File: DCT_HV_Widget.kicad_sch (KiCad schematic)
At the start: 12 parts

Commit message: Updated schematic.
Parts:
- removed D? (x2): BAS21, Package_TO_SOT_SMD:SOT-23, symbol Diode:BAS21
- removed U?: LT1468CS8-PBF, SO-8_S_LIT, symbol LT1468CS8#PBF:LT1468CS8-PBF
- added D1: BAS21SW, symbol Device:D_Dual_Series_ACK_Parallel
- added U?: OC150G, symbol OC150G:OC150G
- added U?: OPAMP, symbol pspice:OPAMP
- gave numbers to parts that had none: 7
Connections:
- net at R4.1: now also C2.1, R2.2, U?.1 (+)
- net at R4.2: now also C2.1
- net VCC: now reaches R3.1
- net VCC: now also R1.1
- net GND: now reaches R3.2
- net GND: now also Q1.3 (C), R2.1, D1.2 (A), U?.3, U?.4 (V+), U?.5 (V-)
- net at C2.2: now also C2.2, Q1.2 (B), U?.3
- net at R?.1: now also Q1.1 (E)
- net at R?.2: now also U?.1
- net at R6.1: now also U?.2 (-)
- net at R6.2: now also R1.2, D1.3 (K)
- new net: U?.2, U?.4
- new net: D1.1 (K), U?.6
- new net HV8k: U?.5
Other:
- moved on the sheet: C2, Q1, R1, R2, R3, R4, R6, R?

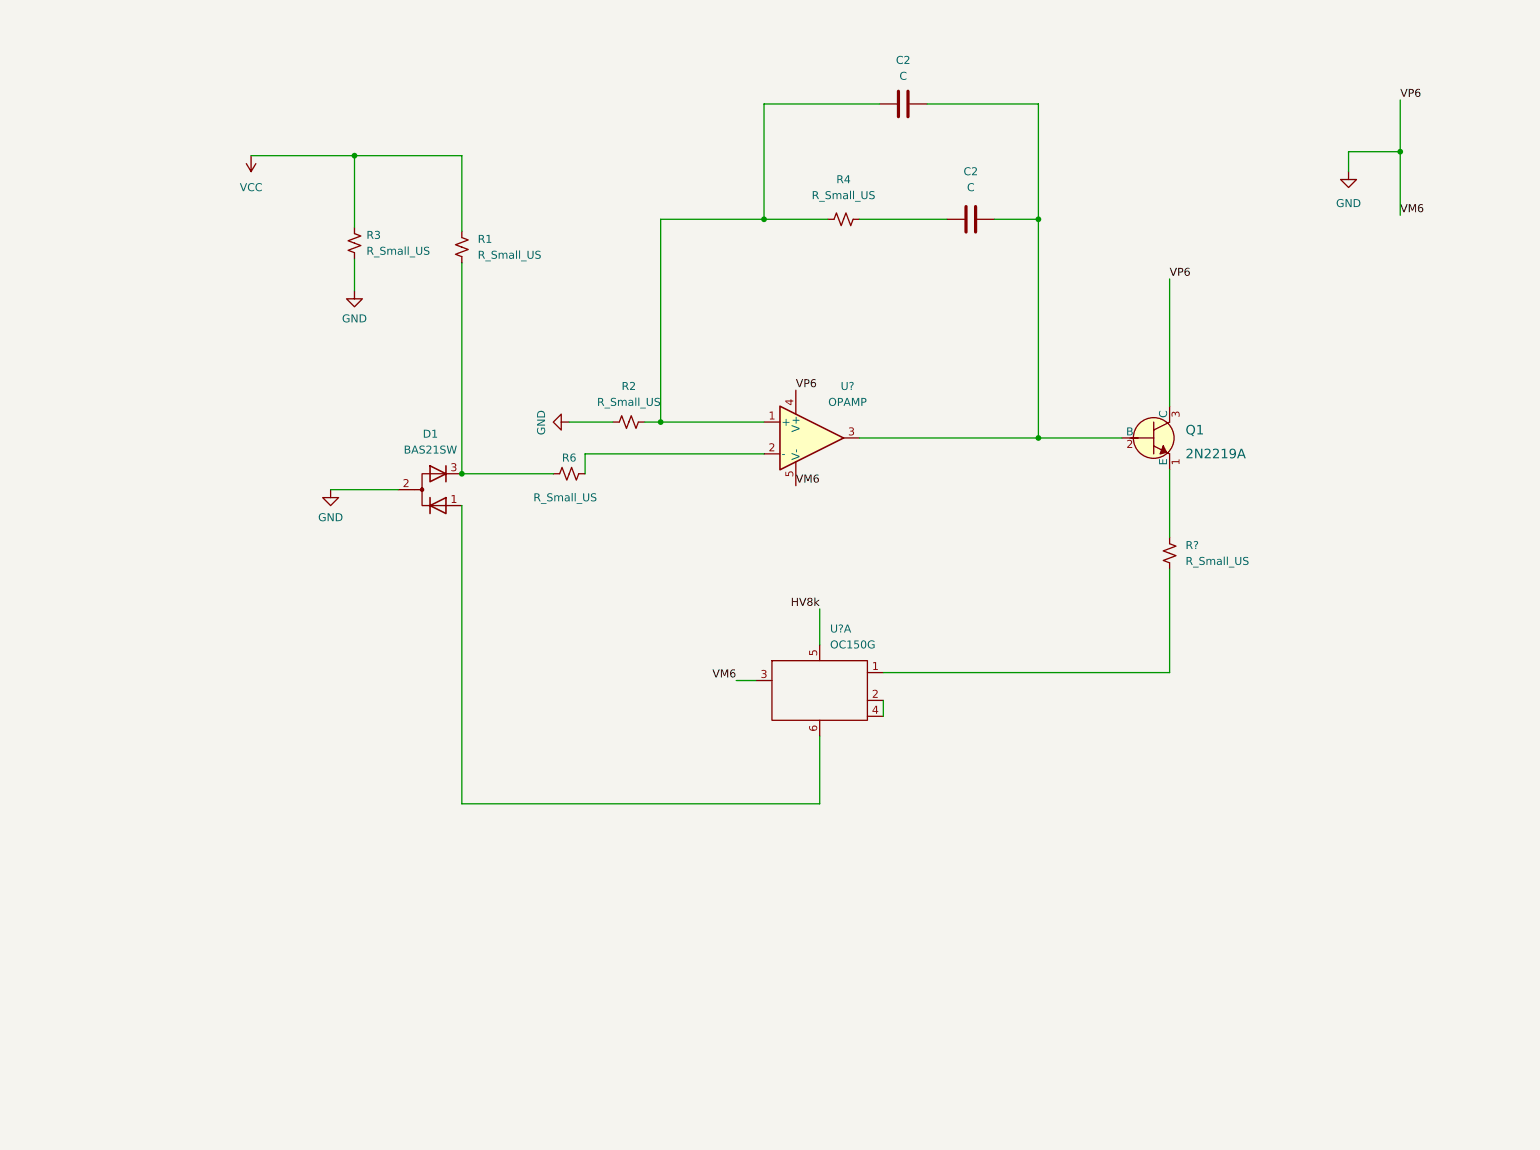
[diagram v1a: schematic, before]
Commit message: Updated schematic connecting pin 3 and pin 1 on BAS21SW diode
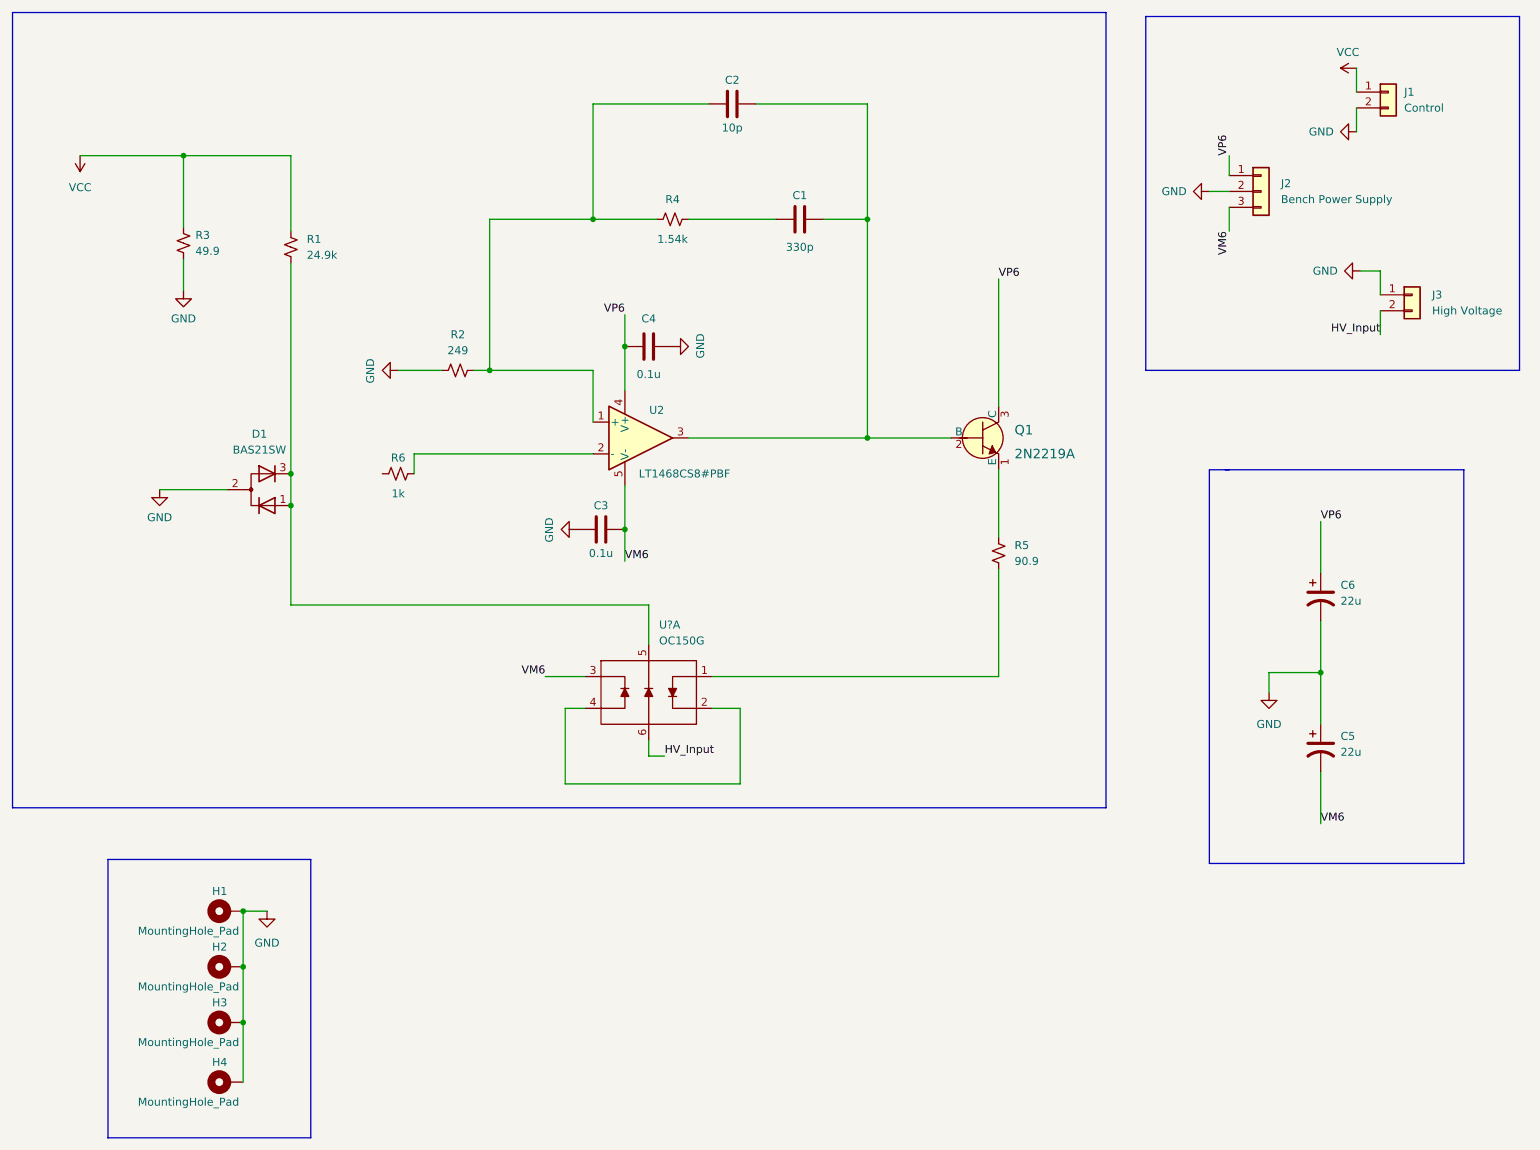
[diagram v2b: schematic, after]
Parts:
- removed U?: OC150G, symbol OC150G:OC150G
- added C3, C4: 0.1u, symbol Device:C
- added C5, C6: 22u, symbol Device:C_Polarized_US
- added H1, H2, H3, H4: MountingHole_Pad, symbol Mechanical:MountingHole_Pad
- added J1: Control, symbol Connector_Generic:Conn_01x02
- added J2: Bench Power Supply, symbol Connector_Generic:Conn_01x03
- added J3: High Voltage, symbol Connector_Generic:Conn_01x02
- added U?: OC150G, symbol OC150G:OC150G
- C1: renamed from C2; value C -> 330p
- C2: value C -> 10p
- R1: value R_Small_US -> 24.9k
- R2: value R_Small_US -> 249
- R3: value R_Small_US -> 49.9
- R4: value R_Small_US -> 1.54k
- R5: renamed from R?; value R_Small_US -> 90.9
- R6: value R_Small_US -> 1k
- U2: renamed from U?; value OPAMP -> LT1468CS8#PBF
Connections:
- net GND: now also C3.1, C4.2, C5.1, C6.2, H1.1, H2.1, H3.1, H4.1, J1.2 (Pin_2), J2.2 (Pin_2), J3.1 (Pin_1); no longer Q1.3 (C), U2.4 (V+), U2.5 (V-)
- net VCC: now also J1.1 (Pin_1)
- net at R5.2: now also U?.1
- net at D1.1 (K): now also D1.3 (K), R1.2, U?.5
- new net: U?.2, U?.4
- new net HV_Input: J3.2 (Pin_2), U?.6
- new net VM6: C3.2, C5.2, J2.3 (Pin_3), U2.5 (V-), U?.3
- new net VP6: C4.1, C6.1, J2.1 (Pin_1), Q1.3 (C), U2.4 (V+)
- now unconnected: R6.2
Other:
- moved on the sheet: C1, C2, Q1, R1, R2, R3, R4, R5, R6, U2

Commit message: Minor change to schematic
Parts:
- Q1: value 2N2219A -> ZXTN10150D
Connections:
- net at D1.1 (K), D1.3 (K), R1.2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: now also R6.2
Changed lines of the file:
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@@
-    (stroke (width 0) (type default) (color 0 0 0 0))
-  )
-  (wire (pts (xy 85.09 89.535) (xy 113.665 89.535))
     (stroke (width 0) (type default) (color 0 0 0 0))
   )
@@
     (stroke (width 0) (type default) (color 0 0 0 0))
   )
-  (wire (pts (xy 85.09 89.535) (xy 85.09 92.71))
-    (stroke (width 0) (type default) (color 0 0 0 0))
-  )
   (wire (pts (xy 132.715 125.095) (xy 178.435 125.095))
     (stroke (width 0) (type default) (color 0 0 0 0))
@@
     (stroke (width 0) (type default) (color 0 0 0 0))
   )
+  (wire (pts (xy 113.665 89.535) (xy 95.885 89.535))
+    (stroke (width 0) (type default) (color 0 0 0 0))
+  )
   (wire (pts (xy 48.26 58.42) (xy 48.26 63.5))
     (stroke (width 0) (type default) (color 0 0 0 0))
@@
     (stroke (width 0) (type default) (color 0 0 0 0))
   )
+  (wire (pts (xy 95.885 92.71) (xy 85.09 92.71))
+    (stroke (width 0) (type default) (color 0 0 0 0))
+  )
+  (wire (pts (xy 65.405 92.71) (xy 80.01 92.71))
+    (stroke (width 0) (type default) (color 0 0 0 0))
+  )
   (wire (pts (xy 229.87 116.205) (xy 229.87 124.46))
     (stroke (width 0) (type default) (color 0 0 0 0))
@@
   )
   (wire (pts (xy 215.265 41.91) (xy 215.265 45.085))
+    (stroke (width 0) (type default) (color 0 0 0 0))
+  )
+  (wire (pts (xy 95.885 89.535) (xy 95.885 92.71))
     (stroke (width 0) (type default) (color 0 0 0 0))
   )
@@
   (symbol (lib_id "dk_Transistors-Bipolar-BJT-Single:2N2219A") (at 175.895 86.995 0) (unit 1)
     (in_bom yes) (on_board yes) (fields_autoplaced)
-    (property "Reference" "Q1" (id 0) (at 180.975 85.725 0)
+    (property "Reference" "Q1" (id 0) (at 180.34 85.725 0)
       (effects (font (size 1.524 1.524)) (justify left))
     )
-    (property "Value" "2N2219A" (id 1) (at 180.975 89.535 0)
+    (property "Value" "ZXTN10150D" (id 1) (at 180.34 89.535 0)
       (effects (font (size 1.524 1.524)) (justify left))
     )
@@
     )
     (path "/8e830ab1-87c7-402f-956c-7d7938416b50"
-      (reference "Q1") (unit 1) (value "2N2219A") (footprint "digikey-footprints:TO-39-3")
+      (reference "Q1") (unit 1) (value "ZXTN10150D") (footprint "digikey-footprints:TO-39-3")
     )
     (path "/d52893e1-9864-4675-8757-03951742d70d"

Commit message: Corrected OpAmp pins and updated LT1468
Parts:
- removed U2: LT1468CS8#PBF, symbol pspice:OPAMP
- added U1: LT1468CS8-PBF, SO-8_S_LIT, symbol LT1468CS8#PBF:LT1468CS8-PBF
- J1: value Control -> Control Voltage
- gave numbers to parts that had none: 1
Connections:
- net VM6: now also U1.4 (V-)
- net VP6: now also U1.7 (V+)
- net at C2.1, R2.2, R4.1: now also U1.2 (-IN)
- net at C1.2, C2.2, Q1.2 (B): now also U1.6 (OUT)
- net at R6.1: now also U1.3 (+IN)
- no-connect marks 0 -> 2
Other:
- note added: "Bench Power Supply"
- note added: "FLoBBr"
- note added: "Mounting Holes"
- note added: "Power Connectors"
- moved on the sheet: C3, C4, Q1

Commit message: Updated OC150G footprint
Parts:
- C1, C2, C3, C4: footprint (none) -> Capacitor_SMD:C_0603_1608Metric
- H1, H2, H3, H4: footprint (none) -> MountingHole:MountingHole_3.2mm_M3_Pad
- Q1: footprint digikey-footprints:TO-39-3 -> (none)
- R1, R2, R3, R4, R5, R6: footprint (none) -> Resistor_SMD:R_0603_1608Metric
- U1: footprint SO-8_S_LIT -> LT1468CS8#PBF:LT1468CS8#PBF_SO-8_S_LIT
- U2: footprint (none) -> DCT_HV_Widget:OC150G

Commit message: Updated PCB layout
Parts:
- C5, C6: footprint (none) -> Capacitor_Tantalum_SMD:CP_EIA-3528-21_Kemet-B
- D1: footprint (none) -> DCT_HV_Widget:BAS21SW
- J1, J3: footprint (none) -> Connector_Molex:Molex_Micro-Fit_3.0_43650-0200_1x02_P3.00mm_Horizontal
- J2: footprint (none) -> Connector_Molex:Molex_Micro-Fit_3.0_43650-0300_1x03_P3.00mm_Horizontal
- Q1: footprint (none) -> DCT_HV_Widget:ZXTN10150DZ
- U2: footprint DCT_HV_Widget:OC150G -> DCT_HV_Widget:OC150G_v2
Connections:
- net GND: now also D1.3 (A); no longer D1.2 (A)
- net at D1.1 (K), R1.2, R6.2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: now also D1.2 (K); no longer D1.3 (K)
- net VCC renamed V_Control
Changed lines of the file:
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@@
     (effects (font (size 1.27 1.27)) (justify left bottom))
+  )
+  (label "V_Control" (at 31.75 41.91 270)
+    (effects (font (size 1.27 1.27)) (justify right bottom))
   )
   (label "VP6" (at 229.87 100.33 0)
@@
     (effects (font (size 1.27 1.27)) (justify left bottom))
   )
+  (label "V_Control" (at 235.585 27.94 180)
+    (effects (font (size 1.27 1.27)) (justify right bottom))
+  )
   (label "VM6" (at 215.265 53.975 270)
     (effects (font (size 1.27 1.27)) (justify right bottom))
@@
   (label "HV_Input" (at 125.095 137.795 0)
     (effects (font (size 1.27 1.27)) (justify left bottom))
+  )
+  (label "V_Input" (at 228.6 40.005 270)
+    (effects (font (size 1.27 1.27)) (justify right bottom))
   )
   (label "VP6" (at 215.265 41.91 90)
@@
     (pin "2")
   )
-  (symbol (lib_id "power:VCC") (at 235.585 27.94 90) (unit 1)
-    (in_bom yes) (on_board yes)
-    (property "Reference" "#PWR0107" (id 0) (at 239.395 27.94 0)
-      (effects (font (size 1.27 1.27)) hide)
-    )
-    (property "Value" "VCC" (id 1) (at 232.41 25.4 90)
-      (effects (font (size 1.27 1.27)) (justify right))
-    )
-    (property "Footprint" "" (id 2) (at 235.585 27.94 0)
-      (effects (font (size 1.27 1.27)) hide)
-    )
-    (property "Datasheet" "" (id 3) (at 235.585 27.94 0)
-      (effects (font (size 1.27 1.27)) hide)
-    )
-    (pin "1")
-  )
   (symbol (lib_id "power:GND") (at 234.95 60.325 0) (unit 1)
     (in_bom yes) (on_board yes)
@@
       (effects (font (size 1.27 1.27)) (justify left))
     )
-    (property "Footprint" "DCT_HV_Widget:OC150G" (id 2) (at 123.571 127.381 0)
+    (property "Footprint" "DCT_HV_Widget:OC150G_v2" (id 2) (at 123.571 127.381 0)
       (effects (font (size 1.27 1.27)) hide)
     )
@@
       (effects (font (size 1.27 1.27)) (justify left))
     )
-    (property "Footprint" "" (id 2) (at 220.345 47.625 0)
+    (property "Footprint" "Connector_Molex:Molex_Micro-Fit_3.0_43650-0300_1x03_P3.00mm_Horizontal" (id 2) (at 220.345 47.625 0)
       (effects (font (size 1.27 1.27)) hide)
     )
@@
       (effects (font (size 1.27 1.27)) (justify left))
     )
-    (property "Footprint" "" (id 2) (at 244.475 64.135 0)
+    (property "Footprint" "Connector_Molex:Molex_Micro-Fit_3.0_43650-0200_1x02_P3.00mm_Horizontal" (id 2) (at 244.475 64.135 0)
       (effects (font (size 1.27 1.27)) hide)
     )
@@
     (property "Reference" "D1" (id 0) (at 60.96 89.535 0))
     (property "Value" "BAS21SW" (id 1) (at 60.325 100.965 0))
-    (property "Footprint" "" (id 2) (at 59.055 95.25 0)
+    (property "Footprint" "DCT_HV_Widget:BAS21SW" (id 2) (at 59.055 95.25 0)
       (effects (font (size 1.27 1.27)) hide)
     )
@@
       (effects (font (size 1.524 1.524)) (justify left))
     )
-    (property "Footprint" "" (id 2) (at 180.975 80.645 0)
+    (property "Footprint" "DCT_HV_Widget:ZXTN10150DZ" (id 2) (at 180.975 80.645 0)
       (effects (font (size 1.524 1.524)) (justify left) hide)
     )
@@
     (pin "2")
     (pin "3")
-  )
-  (symbol (lib_id "power:VCC") (at 31.75 41.91 180) (unit 1)
-    (in_bom yes) (on_board yes) (fields_autoplaced)
-    (property "Reference" "#PWR0110" (id 0) (at 31.75 38.1 0)
-      (effects (font (size 1.27 1.27)) hide)
-    )
-    (property "Value" "VCC" (id 1) (at 31.75 46.99 0))
-    (property "Footprint" "" (id 2) (at 31.75 41.91 0)
-      (effects (font (size 1.27 1.27)) hide)
-    )
-    (property "Datasheet" "" (id 3) (at 31.75 41.91 0)
-      (effects (font (size 1.27 1.27)) hide)
-    )
-    (pin "1")
   )
   (symbol (lib_id "power:GND") (at 48.26 63.5 0) (unit 1)
@@
       (effects (font (size 1.27 1.27)) (justify left))
     )
-    (property "Footprint" "" (id 2) (at 240.665 31.75 0)
+    (property "Footprint" "Connector_Molex:Molex_Micro-Fit_3.0_43650-0200_1x02_P3.00mm_Horizontal" (id 2) (at 240.665 31.75 0)
       (effects (font (size 1.27 1.27)) hide)
     )
@@
       (effects (font (size 1.27 1.27)) (justify left))
     )
-    (property "Footprint" "" (id 2) (at 229.87 112.395 0)
+    (property "Footprint" "Capacitor_Tantalum_SMD:CP_EIA-3528-21_Kemet-B" (id 2) (at 229.87 112.395 0)
       (effects (font (size 1.27 1.27)) hide)
     )
@@
       (effects (font (size 1.27 1.27)) (justify left))
     )
-    (property "Footprint" "" (id 2) (at 229.87 136.525 0)
+    (property "Footprint" "Capacitor_Tantalum_SMD:CP_EIA-3528-21_Kemet-B" (id 2) (at 229.87 136.525 0)
       (effects (font (size 1.27 1.27)) hide)
     )
@@
       (reference "#PWR0106") (unit 1) (value "GND") (footprint "")
     )
-    (path "/57d14982-5bb6-4066-a281-663fb3057bd3"
-      (reference "#PWR0107") (unit 1) (value "VCC") (footprint "")
-    )
     (path "/d7412664-fb55-4327-9567-f6e1a4f37fe6"
       (reference "#PWR0108") (unit 1) (value "GND") (footprint "")
@@
       (reference "#PWR0109") (unit 1) (value "GND") (footprint "")
     )
-    (path "/a7bdbe47-0108-4ab6-a2c9-1cb5ab4bd2e8"
-      (reference "#PWR0110") (unit 1) (value "VCC") (footprint "")
-    )
     (path "/23f6f893-dc24-40ae-95c5-84db8f5f0b0b"
       (reference "#PWR0111") (unit 1) (value "GND") (footprint "")
@@
     )
     (path "/cc10a100-055b-4e9c-97e1-1facb23a1991"
-      (reference "C5") (unit 1) (value "22u") (footprint "")
+      (reference "C5") (unit 1) (value "22u") (footprint "Capacitor_Tantalum_SMD:CP_EIA-3528-21_Kemet-B")
     )
     (path "/c4400881-e5ca-4f2a-be70-c86fa2ddcf32"
-      (reference "C6") (unit 1) (value "22u") (footprint "")
+      (reference "C6") (unit 1) (value "22u") (footprint "Capacitor_Tantalum_SMD:CP_EIA-3528-21_Kemet-B")
     )
     (path "/790c30cd-6531-4300-9b45-833fe1fb861e"
-      (reference "D1") (unit 1) (value "BAS21SW") (footprint "")
+      (reference "D1") (unit 1) (value "BAS21SW") (footprint "DCT_HV_Widget:BAS21SW")
     )
     (path "/1814a377-0806-4e8c-b4a1-f86b9d72b0f6"
@@
     )
     (path "/bdc9f8ac-1856-4424-8824-bbc6c83ee9e4"
-      (reference "J1") (unit 1) (value "Control Voltage") (footprint "")
+      (reference "J1") (unit 1) (value "Control Voltage") (footprint "Connector_Molex:Molex_Micro-Fit_3.0_43650-0200_1x02_P3.00mm_Horizontal")
     )
     (path "/6b30e474-d9ea-4a45-8e0e-1ee5e1f38702"
-      (reference "J2") (unit 1) (value "Bench Power Supply") (footprint "")
+      (reference "J2") (unit 1) (value "Bench Power Supply") (footprint "Connector_Molex:Molex_Micro-Fit_3.0_43650-0300_1x03_P3.00mm_Horizontal")
     )
     (path "/6e5b450c-1a45-4e56-b6dc-f06c19c1d668"
-      (reference "J3") (unit 1) (value "High Voltage") (footprint "")
+      (reference "J3") (unit 1) (value "High Voltage") (footprint "Connector_Molex:Molex_Micro-Fit_3.0_43650-0200_1x02_P3.00mm_Horizontal")
     )
     (path "/8e830ab1-87c7-402f-956c-7d7938416b50"
-      (reference "Q1") (unit 1) (value "ZXTN10150D") (footprint "")
+      (reference "Q1") (unit 1) (value "ZXTN10150D") (footprint "DCT_HV_Widget:ZXTN10150DZ")
     )
     (path "/d52893e1-9864-4675-8757-03951742d70d"
@@
     )
     (path "/63cf86f4-3be6-4dea-9ec7-dae636cb4aca"
-      (reference "U2") (unit 1) (value "OC150G") (footprint "DCT_HV_Widget:OC150G")
-    )
-  )
+      (reference "U2") (unit 1) (value "OC150G") (footprint "DCT_HV_Widget:OC150G_v2")
+    )
+  )
